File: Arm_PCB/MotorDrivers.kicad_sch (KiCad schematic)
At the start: 13 parts, among them U0 TB6560_Board, U1 TB6560_Board, U2 TB6560_Board, U3 TB6560_Board, U4 TB6560_Board, U5 TB6560_Board, U6 TB6560_Board

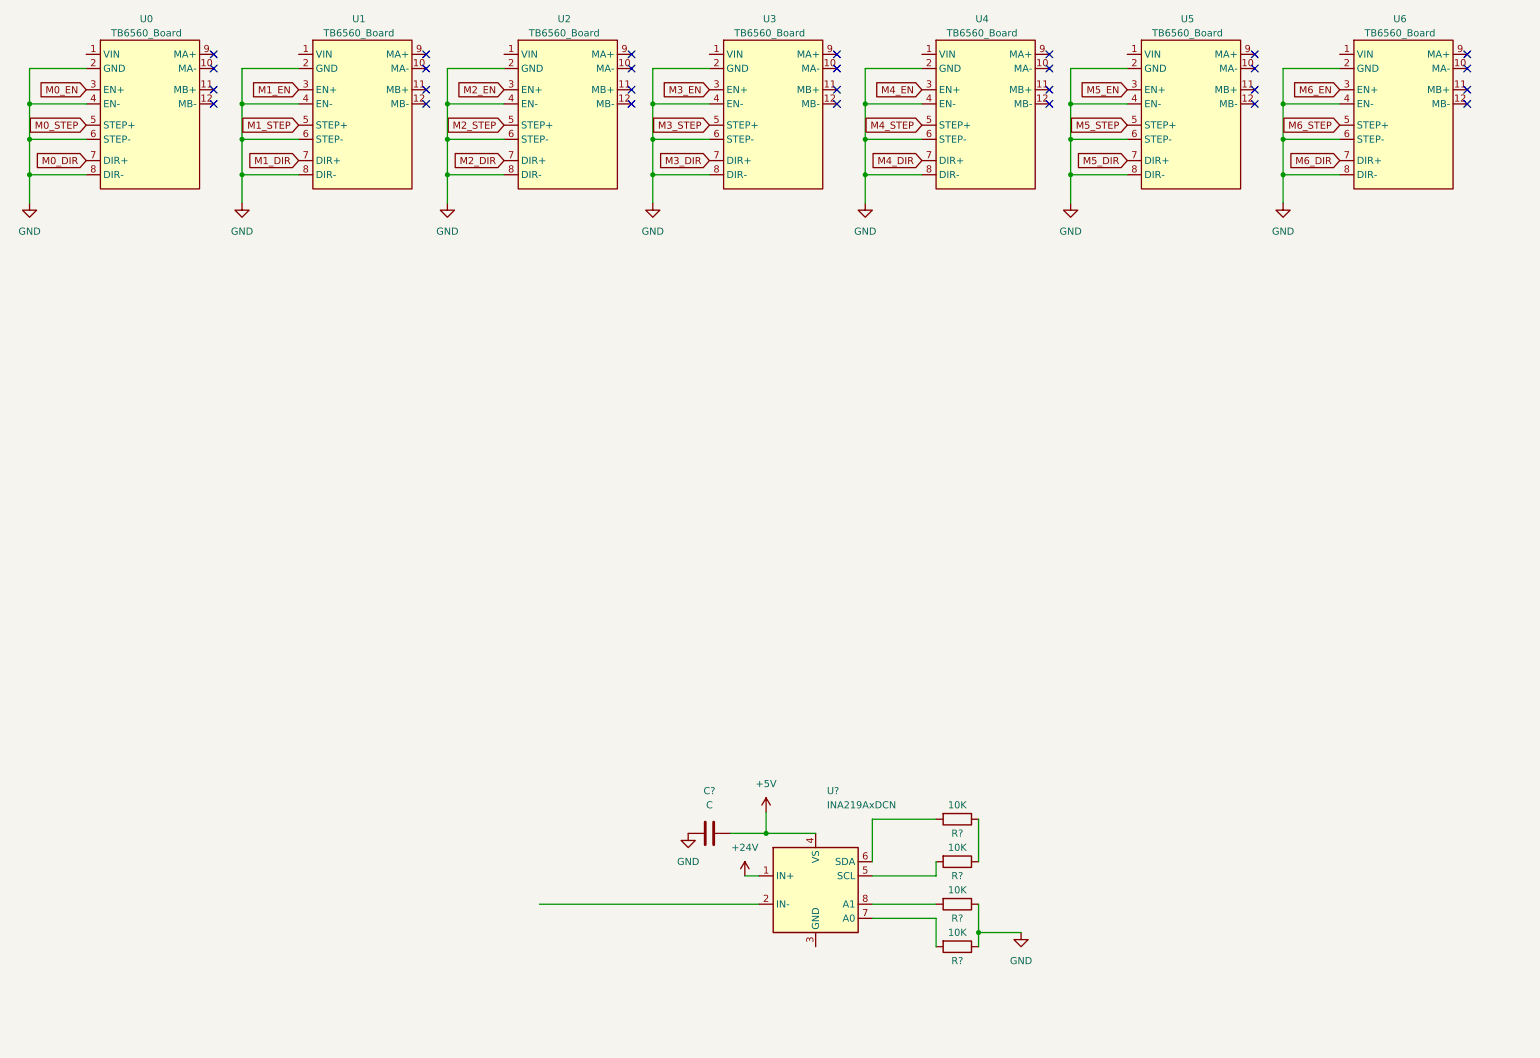
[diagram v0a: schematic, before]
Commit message: Added the INA219 schematics,fixed the TB6560 board, added LED for the EN pin on the microcontroller
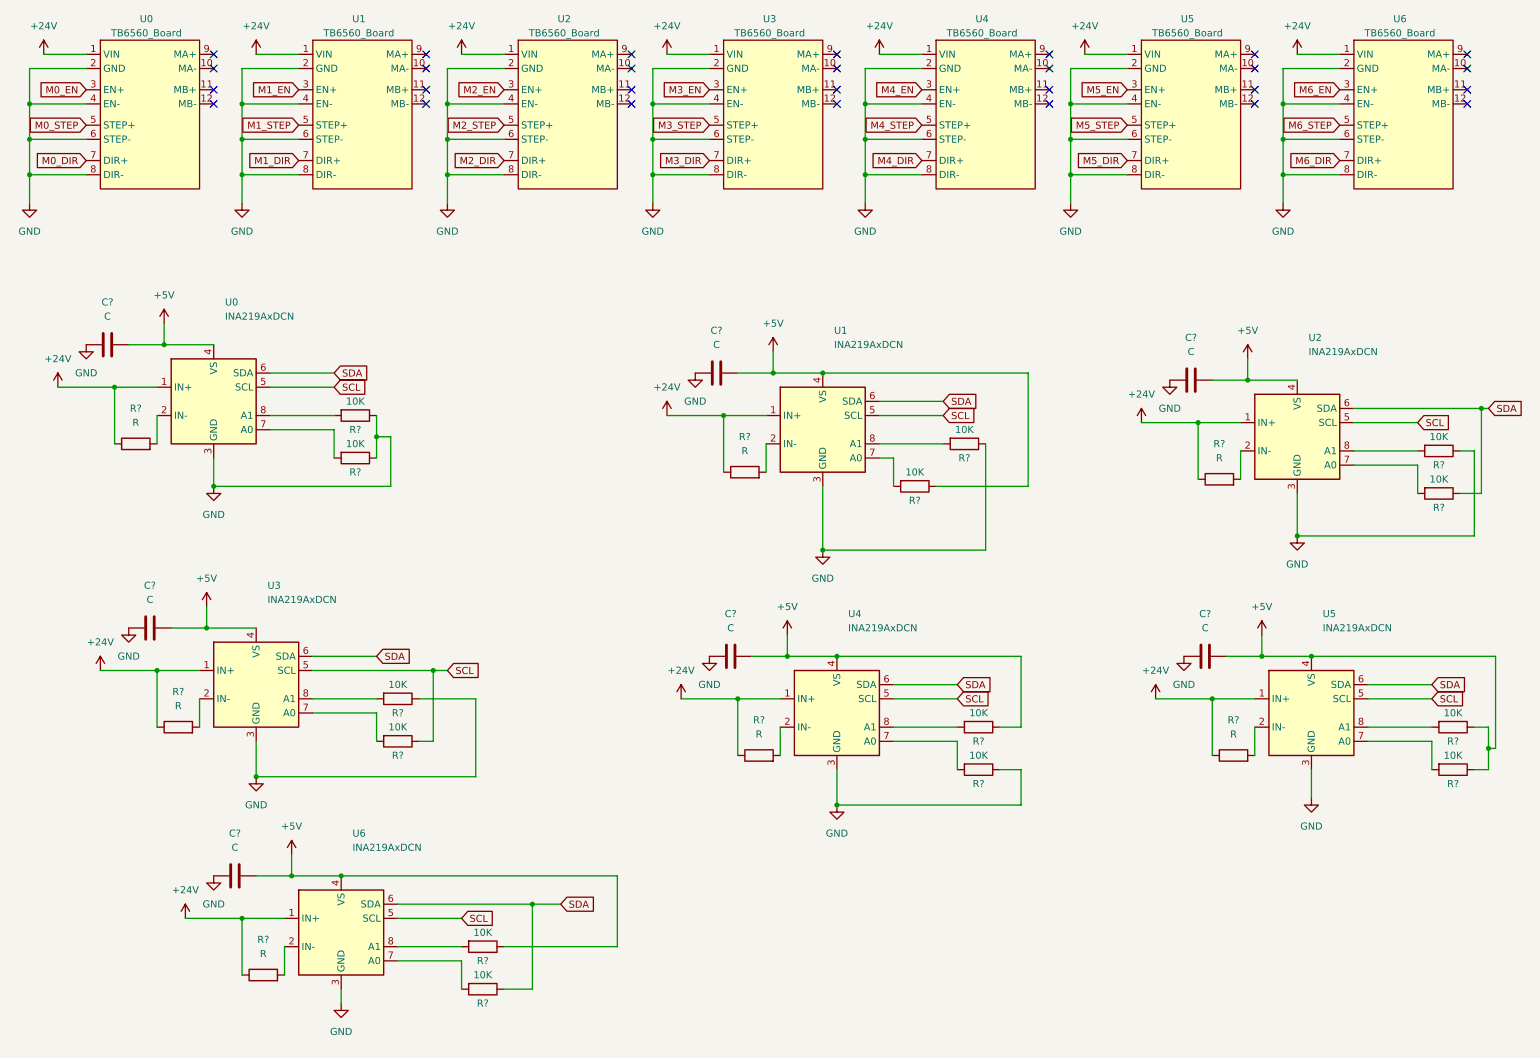
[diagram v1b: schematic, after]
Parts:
- removed R? (x2): 10K, symbol Device:R
- added C? (x6): C, symbol Device:C
- added R? (x12): 10K, symbol Device:R
- added R? (x7): R, symbol Device:R
- added U1, U2, U3, U4, U5, U6: INA219AxDCN, Package_TO_SOT_SMD:SOT-23-8, symbol Sensor_Energy:INA219AxDCN
- gave numbers to parts that had none: 1
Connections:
- net +24V: now also U0.1 (VIN), U1.1 (VIN), U2.1 (VIN), U3.1 (VIN), U4.1 (VIN), U5.1 (VIN), U6.1 (VIN), R?.1, R?.1, R?.1, R?.1, R?.1, R?.1, R?.1, U1.1 (IN+), U2.1 (IN+), U3.1 (IN+), U4.1 (IN+), U5.1 (IN+), U6.1 (IN+)
- net +5V: now also C?.1, C?.1, C?.1, C?.1, C?.1, C?.1, R?.1, R?.1, R?.1, R?.1, R?.1, U1.4 (VS), U2.4 (VS), U3.4 (VS), U4.4 (VS), U5.4 (VS), U6.4 (VS)
- net GND: now also U0.3 (GND), C?.2, C?.2, C?.2, C?.2, C?.2, C?.2, R?.1, R?.1, R?.1, R?.1, U1.3 (GND), U2.3 (GND), U3.3 (GND), U4.3 (GND), U5.3 (GND), U6.3 (GND)
- net at U0.2 (IN-): now also R?.2
- net SCL: now reaches U0.5 (SCL)
- net SCL: now also R?.1, U1.5 (SCL), U2.5 (SCL), U3.5 (SCL), U4.5 (SCL), U5.5 (SCL), U6.5 (SCL)
- net SDA: now reaches U0.6 (SDA)
- net SDA: now also R?.1, R?.1, U1.6 (SDA), U2.6 (SDA), U3.6 (SDA), U4.6 (SDA), U5.6 (SDA), U6.6 (SDA)
- new net: R?.2, U2.8 (A1)
- new net: R?.2, U4.8 (A1)
- new net: R?.2, U6.7 (A0)
- new net: R?.2, U1.2 (IN-)
- new net: R?.2, U1.7 (A0)
- new net: R?.2, U1.8 (A1)
- new net: R?.2, U2.2 (IN-)
- new net: R?.2, U4.2 (IN-)
- new net: R?.2, U4.7 (A0)
- new net: R?.2, U6.8 (A1)
- new net: R?.2, U5.2 (IN-)
- new net: R?.2, U2.7 (A0)
- new net: R?.2, U6.2 (IN-)
- new net: R?.2, U3.8 (A1)
- new net: R?.2, U3.2 (IN-)
- new net: R?.2, U5.7 (A0)
- new net: R?.2, U5.8 (A1)
- new net: R?.2, U3.7 (A0)
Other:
- moved on the sheet: C?, R?, U0

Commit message: Changes
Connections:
- net +24V: no longer U0.1 (VIN), U1.1 (VIN), U2.1 (VIN), U3.1 (VIN), U4.1 (VIN), U5.1 (VIN), U6.1 (VIN)
- net GND: no longer U0.2 (GND), U1.2 (GND), U2.2 (GND), U3.2 (GND), U4.2 (GND), U5.2 (GND), U6.2 (GND)
- net MPOWER1: now reaches R?.2, U1.2 (IN-)
- net MPOWER1: now also U1.1 (VIN)
- net MPOWER2: now reaches R?.2, U2.2 (IN-)
- net MPOWER2: now also U2.1 (VIN)
- net MPOWER4: now reaches R?.2, U4.2 (IN-)
- net MPOWER4: now also U4.1 (VIN)
- net MPOWER0: now reaches R?.2, U0.2 (IN-)
- net MPOWER0: now also U0.1 (VIN)
- net MPOWER5: now reaches R?.2, U5.2 (IN-)
- net MPOWER5: now also U5.1 (VIN)
- net MPOWER6: now reaches R?.2, U6.2 (IN-)
- net MPOWER6: now also U6.1 (VIN)
- net MPOWER3: now reaches R?.2, U3.2 (IN-)
- net MPOWER3: now also U3.1 (VIN)
- new net GNDPWR: U0.2 (GND), U1.2 (GND), U2.2 (GND), U3.2 (GND), U4.2 (GND), U5.2 (GND), U6.2 (GND)
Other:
- note added: "#0: Slave Addr 1000000"
- note added: "#1: Slave Addr 1000001"
- note added: "#2: Slave Addr 1000010"
- note added: "#3: Slave Addr 1000011"
- note added: "#4: Slave Addr 1000100"
- note added: "#5: Slave Addr 1000101"
- note added: "#6: Slave Addr 1000110"
- note added: "Each current sensor goes "above" (by V) the motor driver: IN- to Driver's +24V."
- moved on the sheet: C?, R?, U1, U2, U4, U5, U6

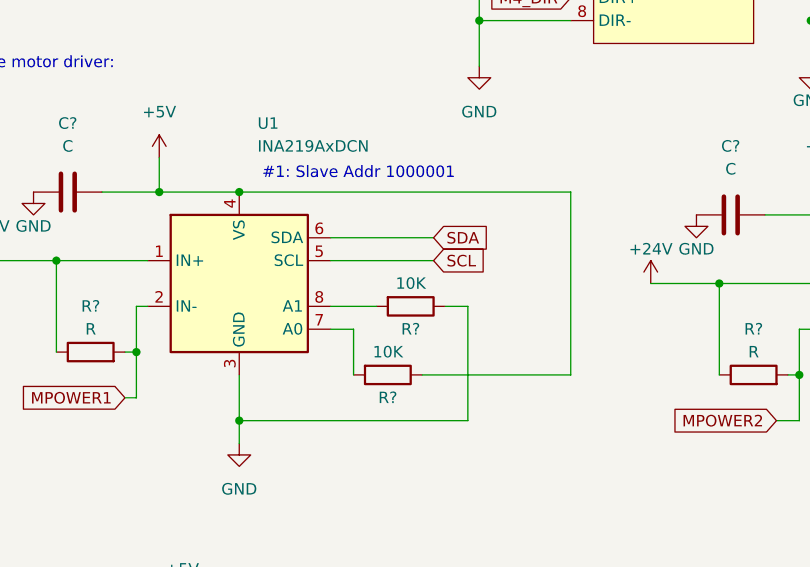
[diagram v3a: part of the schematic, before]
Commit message: Changes, including UX and breakout pins
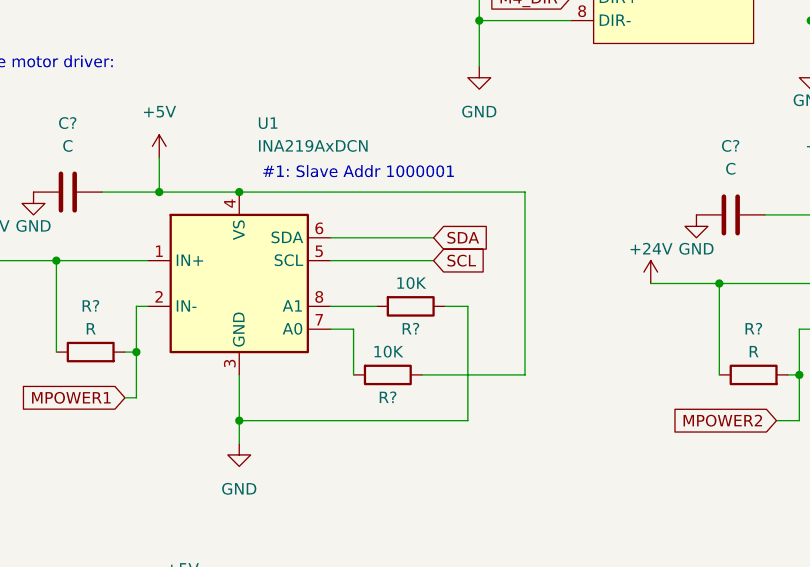
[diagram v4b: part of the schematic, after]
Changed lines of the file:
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@@
     (stroke (width 0) (type default))
   )
-  (wire (pts (xy 167.64 101.6) (xy 167.64 81.28))
+  (wire (pts (xy 162.56 101.6) (xy 162.56 81.28))
     (stroke (width 0) (type default))
   )
@@
     (stroke (width 0) (type default))
   )
-  (wire (pts (xy 167.64 81.28) (xy 130.81 81.28))
+  (wire (pts (xy 162.56 81.28) (xy 130.81 81.28))
     (stroke (width 0) (type default))
   )
@@
     (stroke (width 0) (type default))
   )
-  (wire (pts (xy 151.13 101.6) (xy 167.64 101.6))
-    (stroke (width 0) (type default))
-  )
+  (wire (pts (xy 151.13 101.6) (xy 162.56 101.6))
+    (stroke (width 0) (type default))
+  )

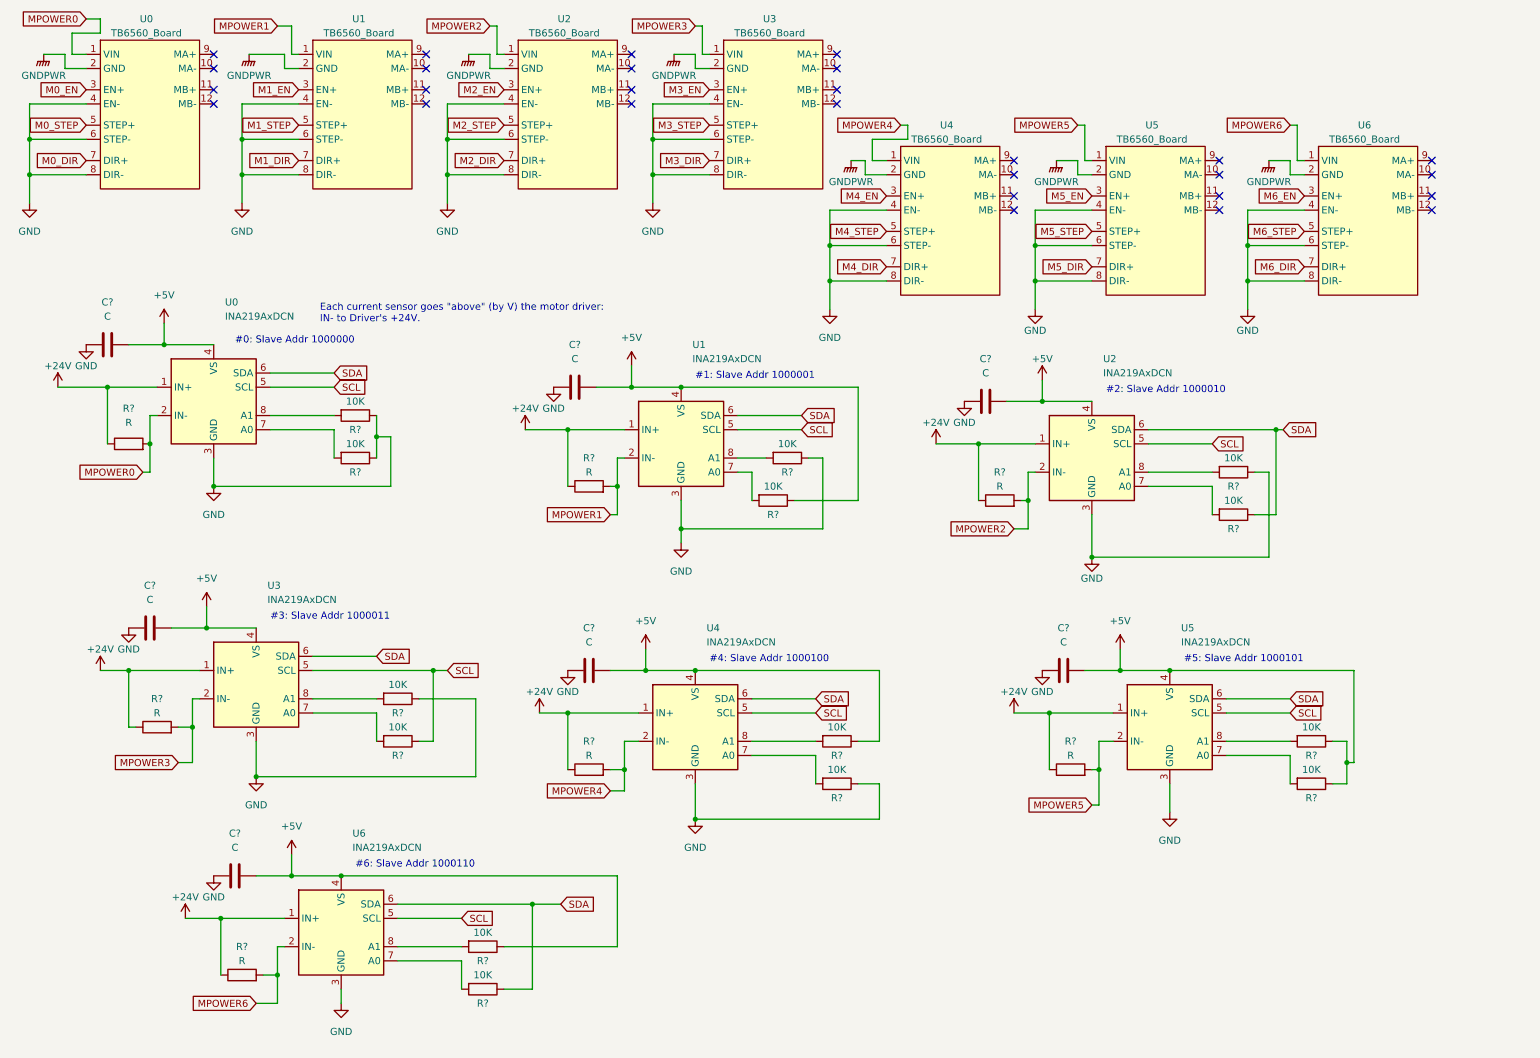
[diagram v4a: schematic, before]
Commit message: Add servo current sensors, etc.
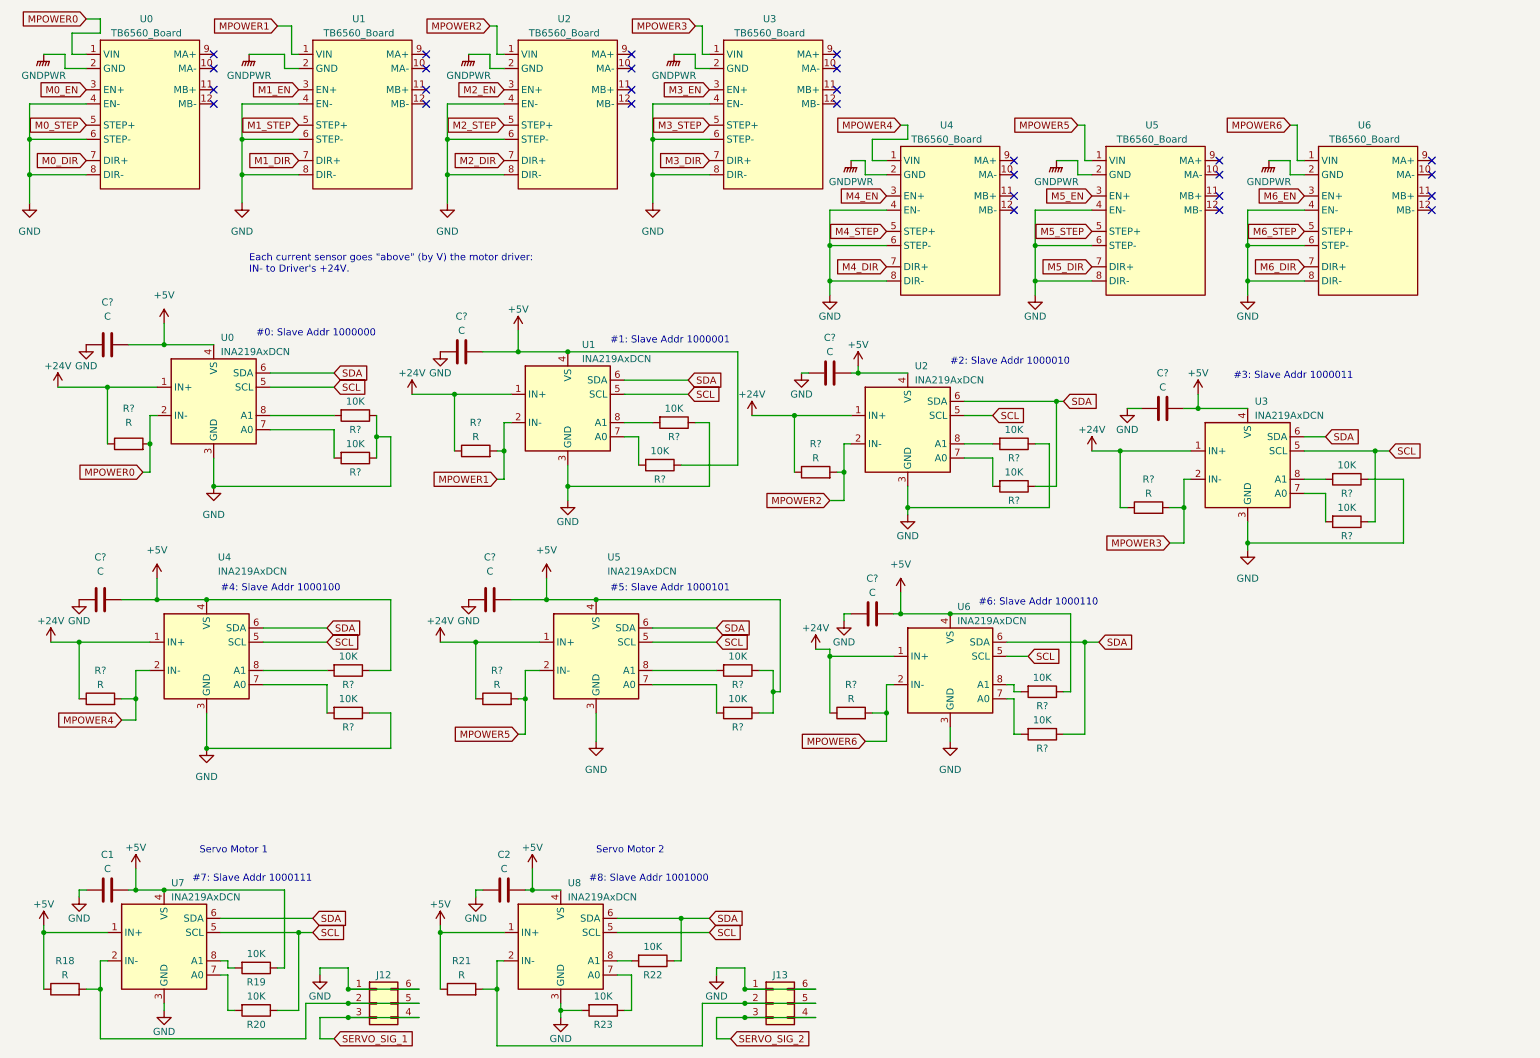
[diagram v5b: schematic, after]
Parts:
- added C1, C2: C, symbol Device:C
- added J12, J13: Conn_02x03_Counter_Clockwise, symbol Connector_Generic:Conn_02x03_Counter_Clockwise
- added R18, R21: R, symbol Device:R
- added R19, R20, R22, R23: 10K, symbol Device:R
- added U7, U8: INA219AxDCN, Package_TO_SOT_SMD:SOT-23-8, symbol Sensor_Energy:INA219AxDCN
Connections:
- net +5V: now also C1.1, C2.1, R18.1, R19.1, R21.1, U7.1 (IN+), U7.4 (VS), U8.1 (IN+), U8.4 (VS)
- net GND: now also C1.2, C2.2, J12.1 (Pin_1), J12.6 (Pin_6), J13.1 (Pin_1), J13.6 (Pin_6), R23.2, U7.3 (GND), U8.3 (GND)
- net SCL: now also R20.1, U7.5 (SCL), U8.5 (SCL)
- net SDA: now also R22.1, U7.6 (SDA), U8.6 (SDA)
- new net: J13.2 (Pin_2), J13.5 (Pin_5), R21.2, U8.2 (IN-)
- new net: R23.1, U8.7 (A0)
- new net: R22.2, U8.8 (A1)
- new net: R20.2, U7.7 (A0)
- new net: R19.2, U7.8 (A1)
- new net: J12.2 (Pin_2), J12.5 (Pin_5), R18.2, U7.2 (IN-)
- new net SERVO_SIG_1: J12.3 (Pin_3), J12.4 (Pin_4)
- new net SERVO_SIG_2: J13.3 (Pin_3), J13.4 (Pin_4)
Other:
- note added: "#7: Slave Addr 1000111"
- note added: "#8: Slave Addr 1001000"
- note added: "Servo Motor 1"
- note added: "Servo Motor 2"
- moved on the sheet: C?, R?, U1, U2, U3, U4, U5, U6
